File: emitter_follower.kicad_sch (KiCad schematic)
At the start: 14 parts, among them Q4001 DNLS350E, Q4002 DPLS350E, Q5003 TIP41C, Q5004 TIP42C

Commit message: move symbols to project specific library
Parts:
- Q4001, Q5003: symbol Transistor_BJT:TIP41C -> pss:TIP41C
- Q4002, Q5004: symbol Transistor_BJT:TIP42C -> pss:TIP42C
- R4001, R4002, R4004, R4005, R4006, R5003: symbol Device:R -> pss:R
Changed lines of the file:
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@@
 	)
 	(symbol
-		(lib_id "Device:R")
+		(lib_id "pss:R")
 		(at 130.81 74.93 90)
 		(unit 1)
@@
 	)
 	(symbol
-		(lib_id "Device:R")
+		(lib_id "pss:R")
 		(at 130.81 125.73 90)
 		(unit 1)
@@
 	)
 	(symbol
-		(lib_id "power:+10V")
+		(lib_id "pss:+10V")
 		(at 160.02 63.5 0)
 		(unit 1)
@@
 	)
 	(symbol
-		(lib_id "Device:R")
+		(lib_id "pss:R")
 		(at 160.02 109.22 0)
 		(unit 1)
@@
 	)
 	(symbol
-		(lib_id "Device:R")
+		(lib_id "pss:R")
 		(at 171.45 109.22 0)
 		(unit 1)
@@
 	)
 	(symbol
-		(lib_id "Device:R")
+		(lib_id "pss:R")
 		(at 171.45 91.44 0)
 		(unit 1)
@@
 	)
 	(symbol
-		(lib_id "Transistor_BJT:TIP42C")
+		(lib_id "pss:TIP42C")
 		(at 149.86 116.84 180)
 		(unit 1)
@@
 	)
 	(symbol
-		(lib_id "Transistor_BJT:TIP41C")
+		(lib_id "pss:TIP41C")
 		(at 157.48 74.93 0)
 		(unit 1)
@@
 	)
 	(symbol
-		(lib_id "Transistor_BJT:TIP41C")
+		(lib_id "pss:TIP41C")
 		(at 149.86 83.82 0)
 		(mirror y)
@@
 	)
 	(symbol
-		(lib_id "power:-5V")
+		(lib_id "pss:-5V")
 		(at 160.02 138.43 180)
 		(unit 1)
@@
 	)
 	(symbol
-		(lib_id "Device:R")
+		(lib_id "pss:R")
 		(at 160.02 91.44 0)
 		(unit 1)
@@
 	)
 	(symbol
-		(lib_id "Transistor_BJT:TIP42C")
+		(lib_id "pss:TIP42C")
 		(at 157.48 125.73 0)
 		(mirror x)

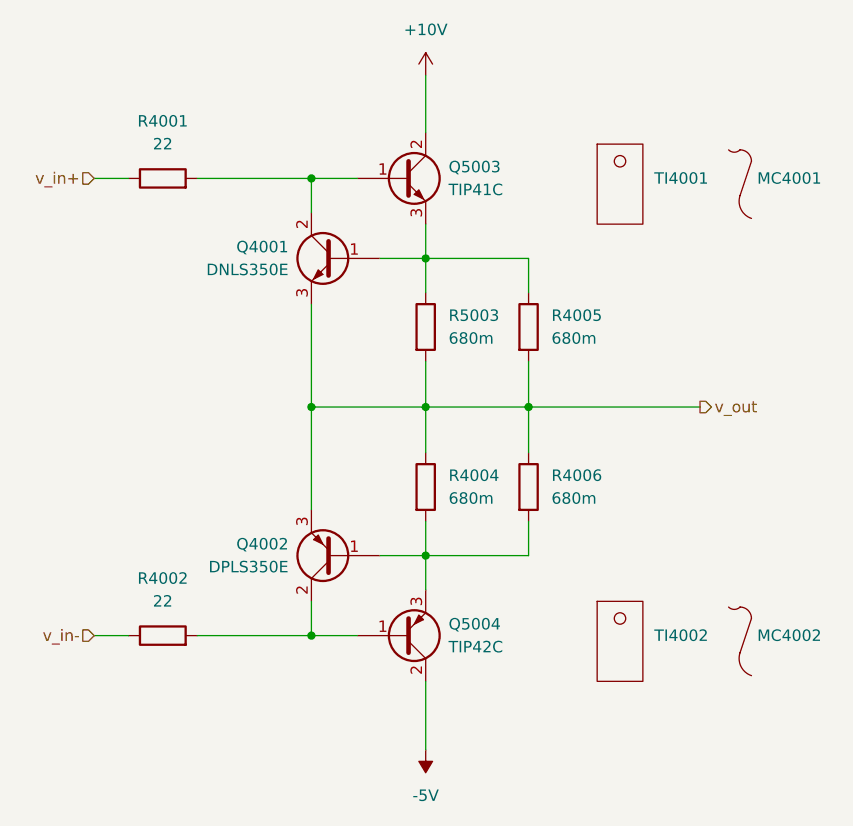
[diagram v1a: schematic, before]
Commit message: refactor schematic hirarchy
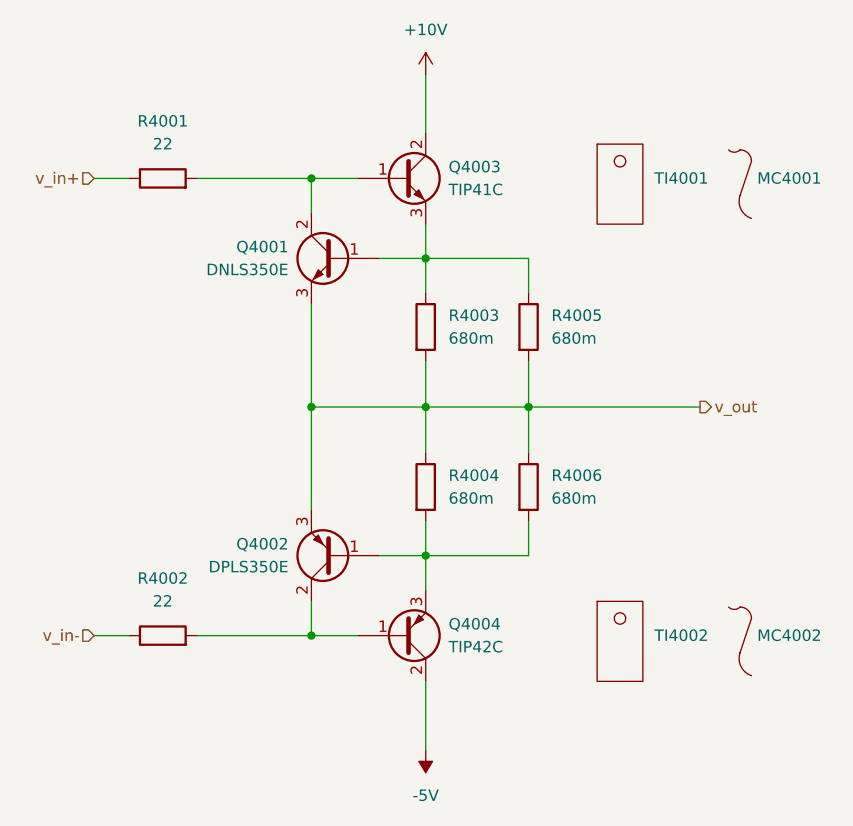
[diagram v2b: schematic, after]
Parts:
- renumbered Q5003 to Q4003, Q5004 to Q4004, R5003 to R4003

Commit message: fix missing footprints, MPN, VPN and datasheet info in BOM
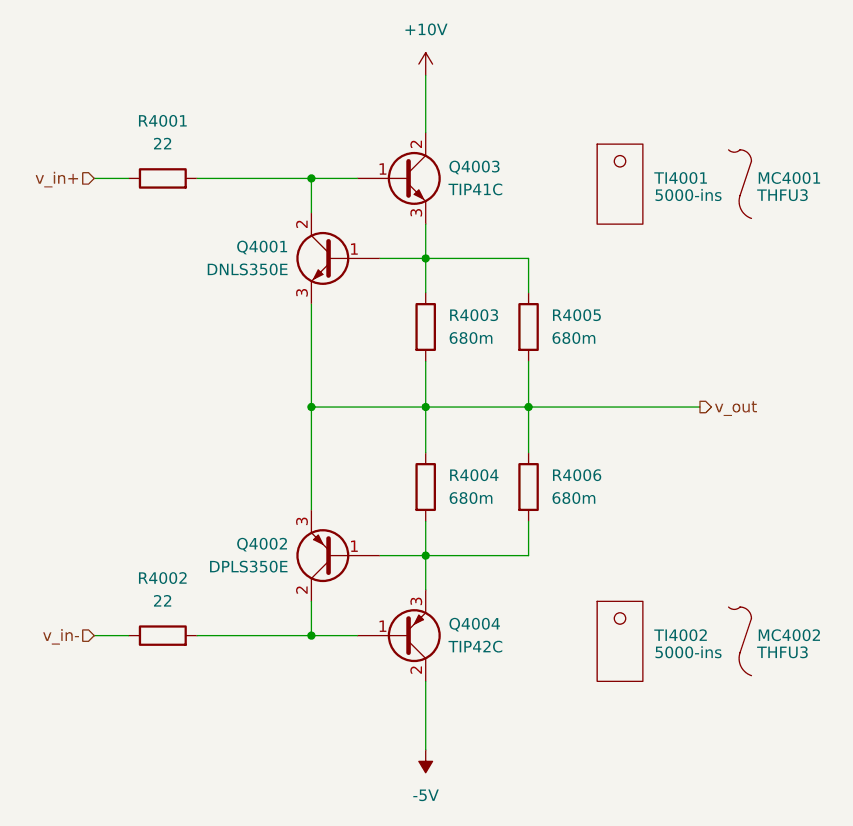
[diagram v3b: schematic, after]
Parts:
- MC4001, MC4002: value ~ -> THFU3; MPN (none) -> THFU 3
- Q4001: footprint Package_TO_SOT_THT:TO-220-3_Vertical -> Package_TO_SOT_SMD:SOT-223-3_TabPin2; MPN (none) -> DNLS350E-13; VPN (none) -> 621-DNLS350E-13
- Q4002: footprint Package_TO_SOT_THT:TO-220-3_Vertical -> Package_TO_SOT_SMD:SOT-223-3_TabPin2; MPN (none) -> DPLS350E-13; VPN (none) -> 621-DPLS350E-13
- Q4003: MPN (none) -> TIP41C; VPN (none) -> 511-TIP41C
- Q4004: MPN (none) -> TIP42C; VPN (none) -> 511-TIP42C
- R4001, R4002: footprint (none) -> Resistor_THT:R_Axial_DIN0617_L17.0mm_D6.0mm_P20.32mm_Horizontal; MPN (none) -> RR03J22RTB; VPN (none) -> 279-RR03J22RTB
- R4003, R4004, R4005, R4006: footprint (none) -> Resistor_THT:R_Axial_DIN0411_L9.9mm_D3.6mm_P12.70mm_Horizontal; MPN (none) -> RR02JR68TB; VPN (none) -> 279-RR02JR68TB
- TI4001, TI4002: value ~ -> 5000-ins; MPN (none) -> A15037003; VPN (none) -> 739-A15037003
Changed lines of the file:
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@@
 			)
 		)
-		(property "Footprint" ""
+		(property "Footprint" "Resistor_THT:R_Axial_DIN0617_L17.0mm_D6.0mm_P20.32mm_Horizontal"
 			(at 130.81 76.708 90)
 			(effects
@@
 			)
 		)
-		(property "Datasheet" "~"
+		(property "Datasheet" "https://www.mouser.de/datasheet/2/418/8/NG_DS_3_1773449_2_E-734389.pdf"
 			(at 130.81 74.93 0)
 			(effects
@@
 			)
 		)
-		(property "MPN" ""
+		(property "MPN" "RR03J22RTB"
 			(at 130.81 74.93 0)
 			(effects
@@
 			)
 		)
-		(property "VPN" ""
+		(property "VPN" "279-RR03J22RTB"
 			(at 130.81 74.93 0)
 			(effects
@@
 			)
 		)
-		(property "Footprint" ""
+		(property "Footprint" "Resistor_THT:R_Axial_DIN0617_L17.0mm_D6.0mm_P20.32mm_Horizontal"
 			(at 130.81 127.508 90)
 			(effects
@@
 			)
 		)
-		(property "Datasheet" "~"
+		(property "Datasheet" "https://www.mouser.de/datasheet/2/418/8/NG_DS_3_1773449_2_E-734389.pdf"
 			(at 130.81 125.73 0)
 			(effects
@@
 			)
 		)
-		(property "MPN" ""
+		(property "MPN" "RR03J22RTB"
 			(at 130.81 125.73 0)
 			(effects
@@
 			)
 		)
-		(property "VPN" ""
+		(property "VPN" "279-RR03J22RTB"
 			(at 130.81 125.73 0)
 			(effects
@@
 			)
 		)
-		(property "Value" "~"
+		(property "Value" "THFU3"
 			(at 196.85 127.635 0)
 			(effects
@@
 			)
 		)
-		(property "Datasheet" ""
+		(property "Datasheet" "https://fischerelektronik.de/web_fischer/en_GB/VA/THFU3/datasheet.xhtml;jsessionid=5770B526AEBA62D4497BB978A14949ED?branch=heatsinks"
 			(at 194.31 125.73 0)
 			(effects
@@
 		)
 		(property "VPN" ""
+			(at 194.31 125.73 0)
+			(effects
+				(font
+					(size 1.27 1.27)
+				)
+				(hide yes)
+			)
+		)
+		(property "MPN" "THFU 3"
 			(at 194.31 125.73 0)
 			(effects
@@
 			)
 		)
-		(property "Footprint" ""
+		(property "Footprint" "Resistor_THT:R_Axial_DIN0411_L9.9mm_D3.6mm_P12.70mm_Horizontal"
 			(at 158.242 109.22 90)
 			(effects
@@
 			)
 		)
-		(property "Datasheet" "~"
+		(property "Datasheet" "https://www.mouser.de/datasheet/2/418/8/NG_DS_3_1773449_2_E-734312.pdf"
 			(at 160.02 109.22 0)
 			(effects
@@
 			)
 		)
-		(property "MPN" ""
+		(property "MPN" "RR02JR68TB"
 			(at 160.02 109.22 0)
 			(effects
@@
 			)
 		)
-		(property "VPN" ""
+		(property "VPN" "279-RR02JR68TB"
 			(at 160.02 109.22 0)
 			(effects
@@
 			)
 		)
-		(property "Footprint" ""
+		(property "Footprint" "Resistor_THT:R_Axial_DIN0411_L9.9mm_D3.6mm_P12.70mm_Horizontal"
 			(at 169.672 109.22 90)
 			(effects
@@
 			)
 		)
-		(property "Datasheet" "~"
+		(property "Datasheet" "https://www.mouser.de/datasheet/2/418/8/NG_DS_3_1773449_2_E-734312.pdf"
 			(at 171.45 109.22 0)
 			(effects
@@
 			)
 		)
-		(property "MPN" ""
+		(property "MPN" "RR02JR68TB"
 			(at 171.45 109.22 0)
 			(effects
@@
 			)
 		)
-		(property "VPN" ""
+		(property "VPN" "279-RR02JR68TB"
 			(at 171.45 109.22 0)
 			(effects
@@
 			)
 		)
-		(property "Footprint" ""
+		(property "Footprint" "Resistor_THT:R_Axial_DIN0411_L9.9mm_D3.6mm_P12.70mm_Horizontal"
 			(at 169.672 91.44 90)
 			(effects
@@
 			)
 		)
-		(property "Datasheet" "~"
+		(property "Datasheet" "https://www.mouser.de/datasheet/2/418/8/NG_DS_3_1773449_2_E-734312.pdf"
 			(at 171.45 91.44 0)
 			(effects
@@
 			)
 		)
-		(property "MPN" ""
+		(property "MPN" "RR02JR68TB"
 			(at 171.45 91.44 0)
 			(effects
@@
 			)
 		)
-		(property "VPN" ""
+		(property "VPN" "279-RR02JR68TB"
 			(at 171.45 91.44 0)
 			(effects
@@
 			)
 		)
-		(property "Footprint" "Package_TO_SOT_THT:TO-220-3_Vertical"
+		(property "Footprint" "Package_TO_SOT_SMD:SOT-223-3_TabPin2"
 			(at 143.51 114.935 0)
 			(effects
@@
 			)
 		)
-		(property "Datasheet" "https://www.centralsemi.com/get_document.php?cmp=1&mergetype=pd&mergepath=pd&pdf_id=TIP42.PDF"
+		(property "Datasheet" "https://www.diodes.com/assets/Datasheets/ds31230.pdf"
 			(at 149.86 116.84 0)
 			(effects
@@
 			)
 		)
-		(property "MPN" ""
+		(property "MPN" "DPLS350E-13"
 			(at 149.86 116.84 0)
 			(effects
@@
 			)
 		)
-		(property "VPN" ""
+		(property "VPN" "621-DPLS350E-13"
 			(at 149.86 116.84 0)
 			(effects
@@
 			)
 		)
-		(property "MPN" ""
+		(property "MPN" "TIP41C"
 			(at 157.48 74.93 0)
 			(effects
@@
 			)
 		)
-		(property "VPN" ""
+		(property "VPN" "511-TIP41C"
 			(at 157.48 74.93 0)
 			(effects
@@
 			)
 		)
-		(property "Value" "~"
+		(property "Value" "5000-ins"
 			(at 185.42 127.635 0)
 			(effects
@@
 			)
 		)
-		(property "Datasheet" ""
+		(property "Datasheet" "https://www.mouser.de/datasheet/2/987/THS_DS_TGARD5000_032515-1634123.pdf"
 			(at 181.61 125.73 0)
 			(effects
@@
 			)
 		)
-		(property "VPN" ""
+		(property "VPN" "739-A15037003"
+			(at 181.61 125.73 0)
+			(effects
+				(font
+					(size 1.27 1.27)
+				)
+				(hide yes)
+			)
+		)
+		(property "MPN" "A15037003"
 			(at 181.61 125.73 0)
 			(effects
@@
 			)
 		)
-		(property "Footprint" "Package_TO_SOT_THT:TO-220-3_Vertical"
+		(property "Footprint" "Package_TO_SOT_SMD:SOT-223-3_TabPin2"
 			(at 143.51 85.725 0)
 			(effects
@@
 			)
 		)
-		(property "Datasheet" "https://www.centralsemi.com/get_document.php?cmp=1&mergetype=pd&mergepath=pd&pdf_id=tip41.PDF"
+		(property "Datasheet" "https://www.diodes.com/assets/Datasheets/ds31231.pdf"
 			(at 149.86 83.82 0)
 			(effects
@@
 			)
 		)
-		(property "MPN" ""
+		(property "MPN" "DNLS350E-13"
 			(at 149.86 83.82 0)
 			(effects
@@
 			)
 		)
-		(property "VPN" ""
+		(property "VPN" "621-DNLS350E-13"
 			(at 149.86 83.82 0)
 			(effects
@@
 			)
 		)
-		(property "Value" "~"
+		(property "Value" "5000-ins"
 			(at 185.42 76.835 0)
 			(effects
@@
 			)
 		)
-		(property "Datasheet" ""
+		(property "Datasheet" "https://www.mouser.de/datasheet/2/987/THS_DS_TGARD5000_032515-1634123.pdf"
 			(at 181.61 74.93 0)
 			(effects
@@
 			)
 		)
-		(property "VPN" ""
+		(property "VPN" "739-A15037003"
+			(at 181.61 74.93 0)
+			(effects
+				(font
+					(size 1.27 1.27)
+				)
+				(hide yes)
+			)
+		)
+		(property "MPN" "A15037003"
 			(at 181.61 74.93 0)
 			(effects
@@
 			)
 		)
-		(property "Footprint" ""
+		(property "Footprint" "Resistor_THT:R_Axial_DIN0411_L9.9mm_D3.6mm_P12.70mm_Horizontal"
 			(at 158.242 91.44 90)
 			(effects
@@
 			)
 		)
-		(property "Datasheet" "~"
+		(property "Datasheet" "https://www.mouser.de/datasheet/2/418/8/NG_DS_3_1773449_2_E-734312.pdf"
 			(at 160.02 91.44 0)
 			(effects
@@
 			)
 		)
-		(property "MPN" ""
+		(property "MPN" "RR02JR68TB"
 			(at 160.02 91.44 0)
 			(effects
@@
 			)
 		)
-		(property "VPN" ""
+		(property "VPN" "279-RR02JR68TB"
 			(at 160.02 91.44 0)
 			(effects
@@
 			)
 		)
-		(property "MPN" ""
+		(property "MPN" "TIP42C"
 			(at 157.48 125.73 0)
 			(effects
@@
 			)
 		)
-		(property "VPN" ""
+		(property "VPN" "511-TIP42C"
 			(at 157.48 125.73 0)
 			(effects
@@
 			)
 		)
-		(property "Value" "~"
+		(property "Value" "THFU3"
 			(at 196.85 76.835 0)
 			(effects
@@
 			)
 		)
-		(property "Datasheet" ""
+		(property "Datasheet" "https://fischerelektronik.de/web_fischer/en_GB/VA/THFU3/datasheet.xhtml;jsessionid=5770B526AEBA62D4497BB978A14949ED?branch=heatsinks"
 			(at 194.31 74.93 0)
 			(effects
@@
 			(at 194.31 74.93 0)
 			(effects
+				(font
+					(size 1.27 1.27)
+				)
+				(hide yes)
+			)
+		)
+		(property "MPN" "THFU 3"
+			(at 194.31 74.93 0)
+			(effects
